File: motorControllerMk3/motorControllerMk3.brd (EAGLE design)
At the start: 54.6 x 49.2 mm, 43 parts, among them J1 AVR_SPI_PRG_6NS, Y1 16MHz

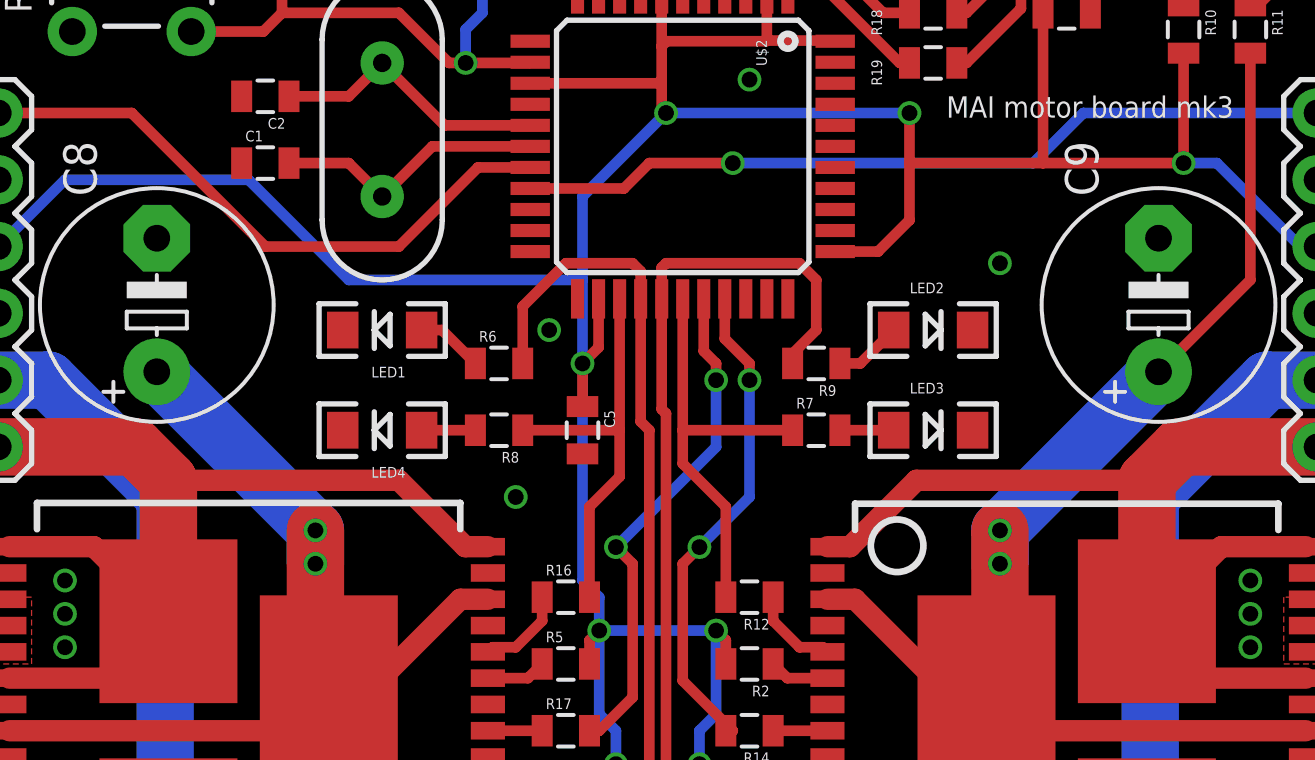
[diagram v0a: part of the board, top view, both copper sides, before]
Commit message: making ground plane bigger
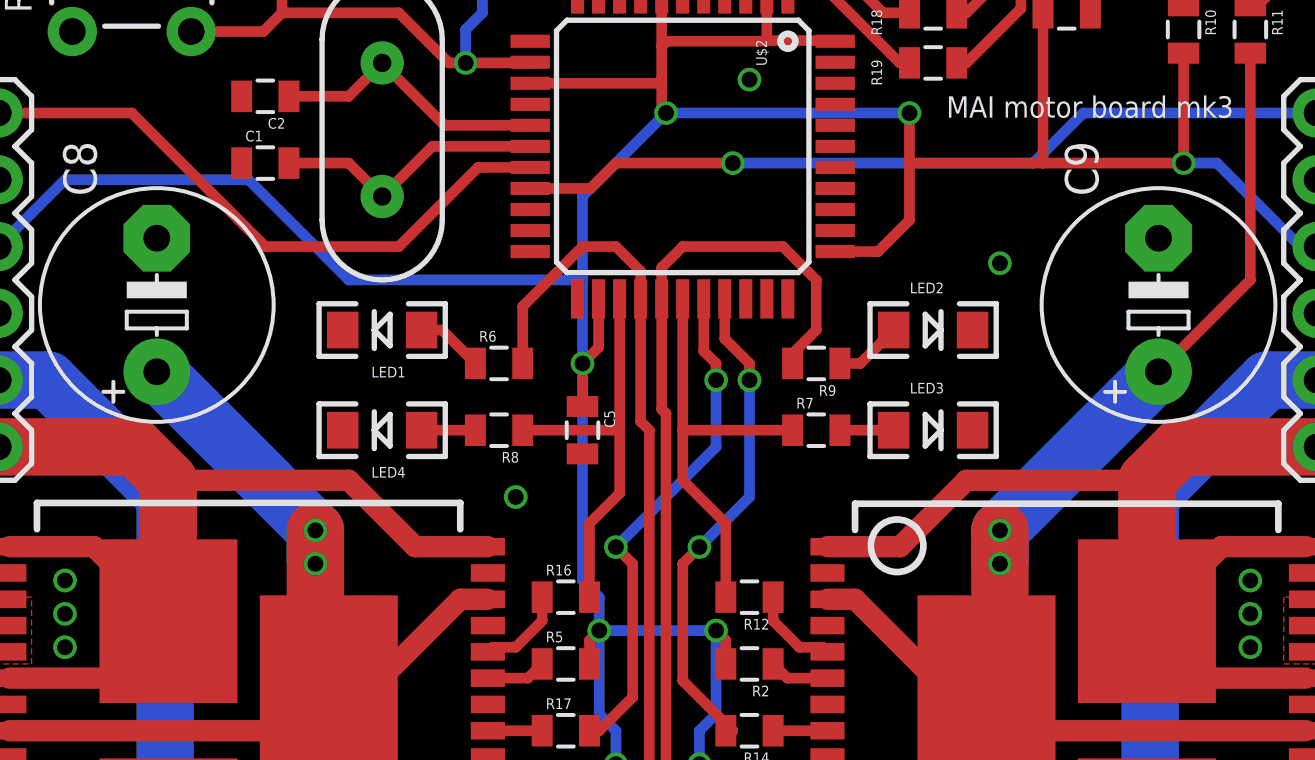
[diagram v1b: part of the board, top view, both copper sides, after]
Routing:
- net PD6: track 31.5 -> 32.0 mm
- net PD7: track 33.8 -> 34.4 mm
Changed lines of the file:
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@@
 <?xml version="1.0" encoding="utf-8"?>
 <!DOCTYPE eagle SYSTEM "eagle.dtd">
-<eagle version="6.3">
+<eagle version="6.5.0">
 <drawing>
 <settings>
@@
 <via x="73.025" y="26.035" extent="1-16" drill="0.6" shape="square"/>
 <via x="73.025" y="27.305" extent="1-16" drill="0.6" shape="square"/>
-<via x="46.355" y="36.83" extent="1-16" drill="0.6" shape="square"/>
 <via x="45.085" y="30.48" extent="1-16" drill="0.6" shape="square"/>
 </signal>
@@
 <wire x1="29.04" y1="28.59" x2="31.875" y2="25.755" width="0.8128" layer="1"/>
 <wire x1="31.89" y1="28.59" x2="31.875" y2="28.575" width="0.8128" layer="1"/>
-<wire x1="44.025" y1="28.59" x2="43.165" y2="28.59" width="0.8128" layer="1"/>
-<wire x1="43.165" y1="28.59" x2="40.64" y2="31.115" width="0.8128" layer="1"/>
-<wire x1="40.64" y1="31.115" x2="31.875" y2="31.115" width="0.8128" layer="1"/>
+<wire x1="44.025" y1="28.59" x2="41.26" y2="28.59" width="0.8128" layer="1"/>
+<wire x1="41.26" y1="28.59" x2="38.735" y2="31.115" width="0.8128" layer="1"/>
+<wire x1="38.735" y1="31.115" x2="31.875" y2="31.115" width="0.8128" layer="1"/>
 <wire x1="25.4" y1="32.385" x2="30.605" y2="32.385" width="2.1844" layer="1"/>
 <wire x1="30.605" y1="32.385" x2="31.875" y2="31.115" width="2.1844" layer="1"/>
@@
 </signal>
 <signal name="PD1">
-<wire x1="49.2" y1="42.215" x2="50.165" y2="43.18" width="0.4064" layer="1"/>
-<wire x1="50.165" y1="43.18" x2="53.34" y2="43.18" width="0.4064" layer="1"/>
+<wire x1="47.93" y1="42.215" x2="48.895" y2="43.18" width="0.4064" layer="1"/>
+<wire x1="48.895" y1="43.18" x2="53.34" y2="43.18" width="0.4064" layer="1"/>
 <via x="53.34" y="43.18" extent="1-16" drill="0.6" shape="square"/>
 <contactref element="JP1" pad="6"/>
 <contactref element="U$2" pad="19"/>
-<wire x1="49.2" y1="42.215" x2="45.635" y2="42.215" width="0.4064" layer="1"/>
+<wire x1="47.93" y1="42.215" x2="45.635" y2="42.215" width="0.4064" layer="1"/>
 <wire x1="53.34" y1="43.18" x2="64.77" y2="43.18" width="0.4064" layer="16"/>
 <wire x1="64.77" y1="43.18" x2="66.675" y2="45.085" width="0.4064" layer="16"/>
@@
 <contactref element="R8" pad="1"/>
 <contactref element="R16" pad="2"/>
-<wire x1="49.035" y1="33.02" x2="49.035" y2="31.255" width="0.4064" layer="1"/>
+<wire x1="49.035" y1="33.02" x2="49.035" y2="30.62" width="0.4064" layer="1"/>
 <wire x1="45.35" y1="33.02" x2="49.035" y2="33.02" width="0.4064" layer="1"/>
 <contactref element="U$2" pad="25"/>
 <wire x1="49.035" y1="38.015" x2="49.035" y2="33.02" width="0.4064" layer="1"/>
-<wire x1="47.89" y1="26.67" x2="47.89" y2="30.11" width="0.4064" layer="1"/>
-<wire x1="47.89" y1="30.11" x2="49.035" y2="31.255" width="0.4064" layer="1"/>
+<wire x1="47.89" y1="26.67" x2="47.89" y2="29.475" width="0.4064" layer="1"/>
+<wire x1="47.89" y1="29.475" x2="49.035" y2="30.62" width="0.4064" layer="1"/>
 </signal>
 <signal name="PB4">
 <contactref element="R7" pad="1"/>
 <contactref element="R12" pad="2"/>
-<wire x1="51.435" y1="33.02" x2="51.435" y2="31.75" width="0.4064" layer="1"/>
+<wire x1="51.435" y1="33.02" x2="51.435" y2="31.115" width="0.4064" layer="1"/>
 <wire x1="55.615" y1="33.02" x2="51.435" y2="33.02" width="0.4064" layer="1"/>
 <contactref element="U$2" pad="28"/>
 <wire x1="51.435" y1="38.015" x2="51.435" y2="33.02" width="0.4064" layer="1"/>
-<wire x1="53.075" y1="26.67" x2="53.075" y2="30.11" width="0.4064" layer="1"/>
-<wire x1="53.075" y1="30.11" x2="51.435" y2="31.75" width="0.4064" layer="1"/>
+<wire x1="53.075" y1="26.67" x2="53.075" y2="29.475" width="0.4064" layer="1"/>
+<wire x1="53.075" y1="29.475" x2="51.435" y2="31.115" width="0.4064" layer="1"/>
 </signal>
 <signal name="PD6">
@@
 <wire x1="50.165" y1="19.05" x2="47.625" y2="16.51" width="0.4064" layer="1"/>
 <wire x1="47.625" y1="16.51" x2="47.89" y2="16.51" width="0.4064" layer="1"/>
-<wire x1="49.835" y1="39.065" x2="49.53" y2="39.37" width="0.4064" layer="1"/>
-<wire x1="49.53" y1="39.37" x2="46.99" y2="39.37" width="0.4064" layer="1"/>
+<wire x1="49.835" y1="39.065" x2="48.895" y2="40.005" width="0.4064" layer="1"/>
+<wire x1="48.895" y1="40.005" x2="47.625" y2="40.005" width="0.4064" layer="1"/>
 <contactref element="U$2" pad="26"/>
 <wire x1="49.835" y1="38.015" x2="49.835" y2="39.065" width="0.4064" layer="1"/>
 <wire x1="49.835" y1="33.35" x2="49.835" y2="38.015" width="0.4064" layer="1"/>
 <wire x1="45.35" y1="35.56" x2="45.35" y2="37.73" width="0.4064" layer="1"/>
-<wire x1="45.35" y1="37.73" x2="46.99" y2="39.37" width="0.4064" layer="1"/>
+<wire x1="45.35" y1="37.73" x2="47.625" y2="40.005" width="0.4064" layer="1"/>
 </signal>
 <signal name="PD7">
@@
 <wire x1="55.615" y1="35.93" x2="56.515" y2="36.83" width="0.4064" layer="1"/>
 <wire x1="56.515" y1="36.83" x2="56.515" y2="38.735" width="0.4064" layer="1"/>
-<wire x1="56.515" y1="38.735" x2="55.88" y2="39.37" width="0.4064" layer="1"/>
-<wire x1="55.88" y1="39.37" x2="50.8" y2="39.37" width="0.4064" layer="1"/>
+<wire x1="56.515" y1="38.735" x2="55.245" y2="40.005" width="0.4064" layer="1"/>
+<wire x1="55.245" y1="40.005" x2="51.435" y2="40.005" width="0.4064" layer="1"/>
 <wire x1="50.635" y1="38.015" x2="50.635" y2="39.205" width="0.4064" layer="1"/>
-<wire x1="50.635" y1="39.205" x2="50.8" y2="39.37" width="0.4064" layer="1"/>
+<wire x1="50.635" y1="39.205" x2="51.435" y2="40.005" width="0.4064" layer="1"/>
 </signal>
 <signal name="N$22">
@@
 <wire x1="71.925" y1="28.59" x2="69.09" y2="25.755" width="0.8128" layer="1"/>
 <wire x1="69.075" y1="28.59" x2="69.09" y2="28.575" width="0.8128" layer="1"/>
-<wire x1="56.94" y1="28.59" x2="57.8" y2="28.59" width="0.8128" layer="1"/>
-<wire x1="57.8" y1="28.59" x2="60.325" y2="31.115" width="0.8128" layer="1"/>
-<wire x1="60.325" y1="31.115" x2="69.09" y2="31.115" width="0.8128" layer="1"/>
+<wire x1="56.94" y1="28.59" x2="59.705" y2="28.59" width="0.8128" layer="1"/>
+<wire x1="59.705" y1="28.59" x2="62.23" y2="31.115" width="0.8128" layer="1"/>
+<wire x1="62.23" y1="31.115" x2="69.09" y2="31.115" width="0.8128" layer="1"/>
 <wire x1="75.565" y1="32.385" x2="70.36" y2="32.385" width="2.1844" layer="1"/>
 <wire x1="70.36" y1="32.385" x2="69.09" y2="31.115" width="2.1844" layer="1"/>

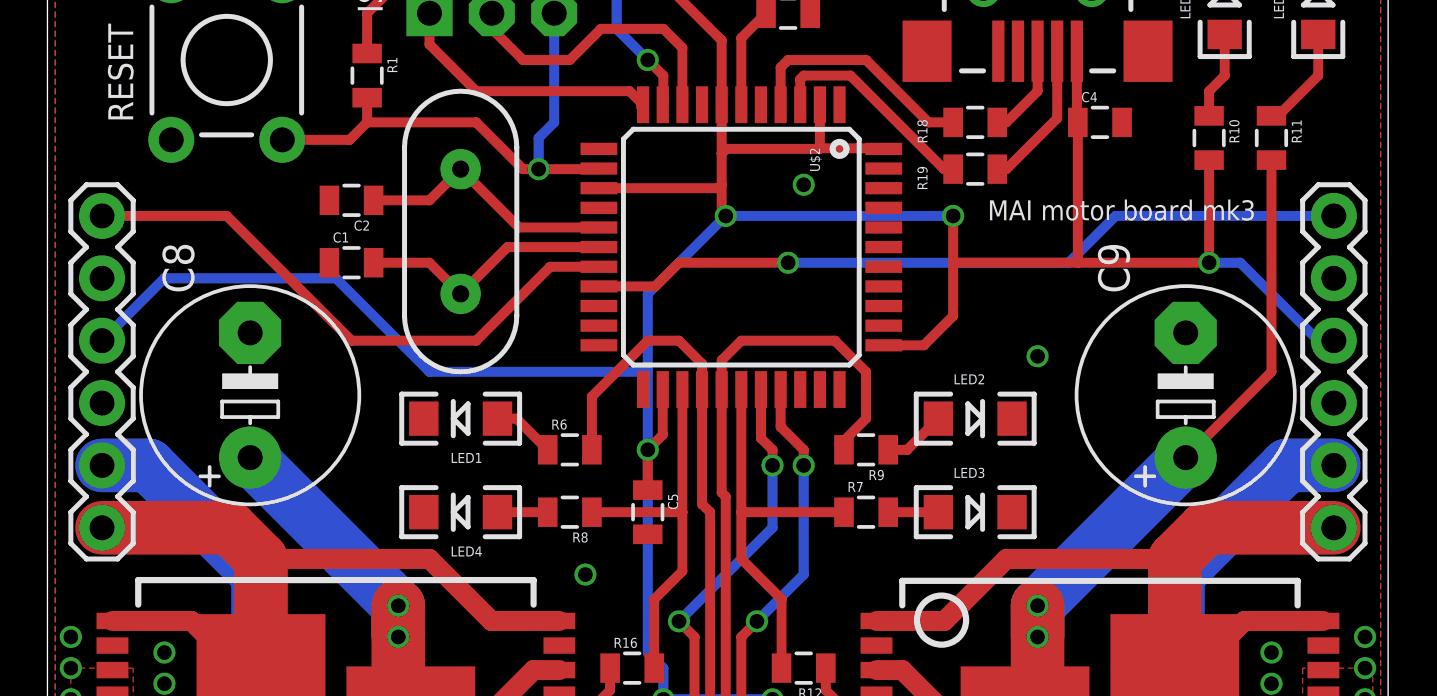
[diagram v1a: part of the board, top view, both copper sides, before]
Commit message: making better silkscreen
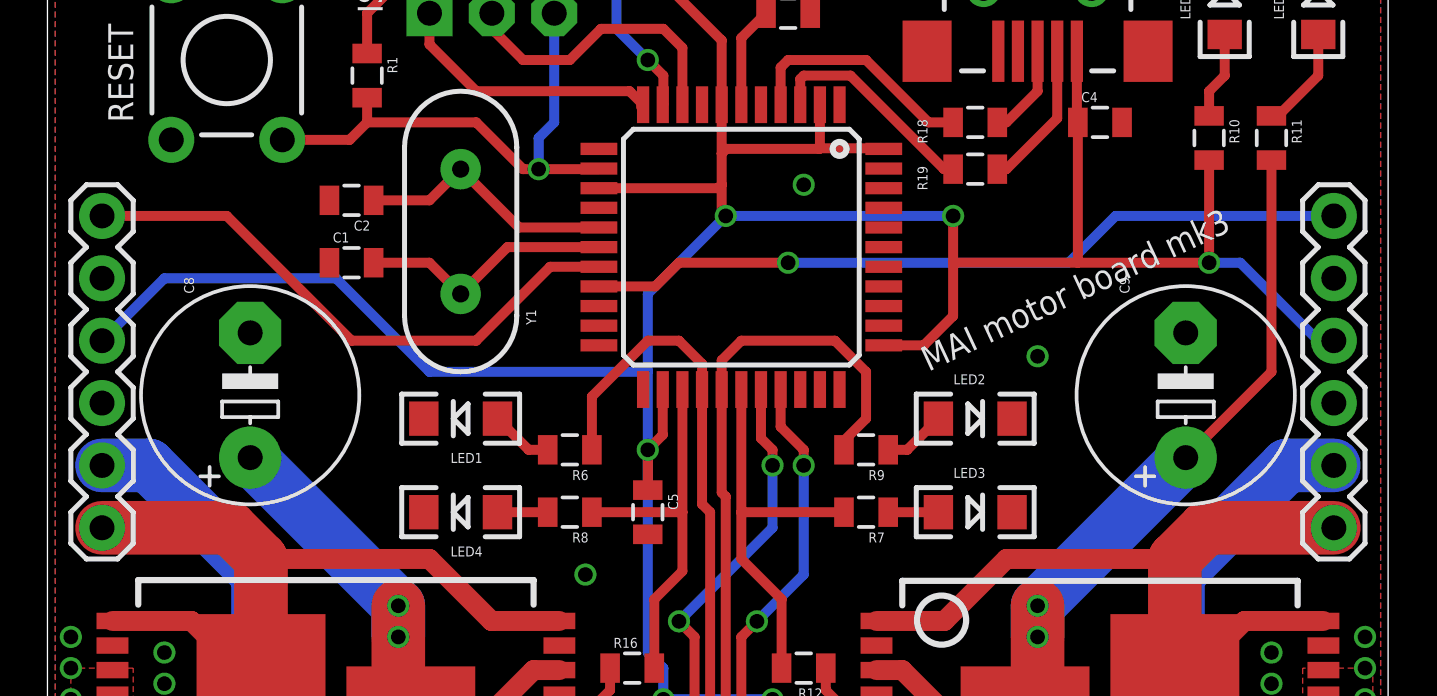
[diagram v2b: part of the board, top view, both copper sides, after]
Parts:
- turned R6 to 180 degrees
- turned R7 to 180 degrees
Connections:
- removed net N$27: LED3.A, R7.2
- removed net N$31: LED1.A, R6.1
- new net N$16: LED3.A, R7.1
- new net N$18: LED1.A, R6.2
- net PB4: now also R7.2; no longer R7.1
- net PD6: now also R6.1; no longer R6.2
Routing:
- net N$31: track 2.57 -> 0.00 mm
- net N$18: track 0.00 -> 2.57 mm
- net N$27: track 2.05 -> 0.00 mm
- net N$16: track 0.00 -> 2.05 mm
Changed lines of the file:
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@@
 <text x="36.83" y="53.34" size="1.016" layer="25" rot="R90">ISP</text>
 <text x="26.67" y="48.895" size="1.016" layer="25" rot="R90">RESET</text>
-<text x="72.39" y="45.72" size="0.8128" layer="21" font="vector" rot="R180">MAI motor board mk3</text>
+<text x="59.055" y="38.735" size="1.016" layer="21" font="vector" rot="R25">MAI motor board mk3</text>
 </plain>
 <attributes>
@@
 <element name="LED3" library="SparkFun-LED" package="LED-1206" value="A1" x="60.96" y="33.02"/>
 <element name="LED4" library="SparkFun-LED" package="LED-1206" value="B2" x="40.005" y="33.02" rot="R180"/>
-<element name="R6" library="SparkFun-Passives" package="0805" value="1k" x="44.45" y="35.56"/>
-<element name="R7" library="SparkFun-Passives" package="0805" value="1k" x="56.515" y="33.02"/>
+<element name="R6" library="SparkFun-Passives" package="0805" value="1k" x="44.45" y="35.56" rot="R180"/>
+<element name="R7" library="SparkFun-Passives" package="0805" value="1k" x="56.515" y="33.02" rot="R180"/>
 <element name="R8" library="SparkFun-Passives" package="0805" value="1k" x="44.45" y="33.02" rot="R180"/>
 <element name="R9" library="SparkFun-Passives" package="0805" value="1k" x="56.515" y="35.56" rot="R180"/>
@@
 <element name="R16" library="SparkFun-Passives" package="0805" value="1k" x="46.99" y="26.67"/>
 <element name="R17" library="SparkFun-Passives" package="0805" value="1k" x="46.99" y="21.59"/>
-<element name="C8" library="rcl" package="E5-8,5" value="2200u" x="31.4325" y="37.7825" rot="R90"/>
-<element name="C9" library="rcl" package="E5-8,5" value="2200u" x="69.5325" y="37.7825" rot="R90"/>
+<element name="C8" library="rcl" package="E5-8,5" value="2200u" x="31.4325" y="37.7825" smashed="yes" rot="R90">
+<attribute name="NAME" x="29.1465" y="41.9227" size="0.4064" layer="25" ratio="10" rot="R90"/>
+<attribute name="VALUE" x="34.4551" y="35.2679" size="0.4064" layer="27" ratio="10" rot="R90"/>
+</element>
+<element name="C9" library="rcl" package="E5-8,5" value="2200u" x="69.5325" y="37.7825" smashed="yes" rot="R90">
+<attribute name="NAME" x="67.2465" y="41.9227" size="0.4064" layer="25" ratio="10" rot="R90"/>
+<attribute name="VALUE" x="72.5551" y="35.2679" size="0.4064" layer="27" ratio="10" rot="R90"/>
+</element>
 <element name="JP1" library="SparkFun-Connectors" package="1X06" value="m1" x="75.565" y="32.385" smashed="yes" rot="R90"/>
 <element name="JP2" library="SparkFun-Connectors" package="1X06" value="m2" x="25.4" y="32.385" smashed="yes" rot="R90"/>
-<element name="U$2" library="SparkFun-DigitalIC" package="SPARKFUN-DIGITALIC_TQFP44" value="ATMEGA32U4TQFP" x="51.435" y="43.815" rot="R270">
+<element name="U$2" library="SparkFun-DigitalIC" package="SPARKFUN-DIGITALIC_TQFP44" value="ATMEGA32U4TQFP" x="51.435" y="43.815" smashed="yes" rot="R270">
 <attribute name="PROD_ID" value="IC-11161" x="51.435" y="43.815" size="1.778" layer="27" rot="R270" display="off"/>
+<attribute name="VALUE" x="47.371" y="47.879" size="0.4064" layer="27" rot="R270"/>
 </element>
 <element name="S2" library="SparkFun-Electromechanical" package="TACTILE-PTH" value="SWITCH-MOMENTARY-2PTH" x="30.48" y="51.435" smashed="yes" rot="R90"/>
-<element name="Y1" library="SparkFun-FreqCtrl" package="HC49US" value="16MHz" x="40.005" y="44.45" smashed="yes" rot="R270"/>
+<element name="Y1" library="SparkFun-FreqCtrl" package="HC49US" value="16MHz" x="40.005" y="44.45" smashed="yes" rot="R270">
+<attribute name="VALUE" x="36.703" y="41.91" size="0.4064" layer="27" ratio="10" rot="R270"/>
+<attribute name="NAME" x="42.672" y="41.275" size="0.4064" layer="25" ratio="10" rot="R270"/>
+</element>
 <element name="U$1" library="SparkFun-PowerIC" package="VNH2SP30" value="VNH2SP30" x="34.925" y="21.59" smashed="yes" rot="R90"/>
 <element name="U$3" library="SparkFun-PowerIC" package="VNH2SP30" value="VNH2SP30" x="66.04" y="21.59" smashed="yes" rot="R270"/>
@@
 </signal>
 <signal name="PB4">
-<contactref element="R7" pad="1"/>
 <contactref element="R12" pad="2"/>
-<wire x1="51.435" y1="33.02" x2="51.435" y2="31.115" width="0.4064" layer="1"/>
-<wire x1="55.615" y1="33.02" x2="51.435" y2="33.02" width="0.4064" layer="1"/>
 <contactref element="U$2" pad="28"/>
 <wire x1="51.435" y1="38.015" x2="51.435" y2="33.02" width="0.4064" layer="1"/>
+<wire x1="51.435" y1="33.02" x2="51.435" y2="31.115" width="0.4064" layer="1"/>
 <wire x1="53.075" y1="26.67" x2="53.075" y2="29.475" width="0.4064" layer="1"/>
 <wire x1="53.075" y1="29.475" x2="51.435" y2="31.115" width="0.4064" layer="1"/>
+<contactref element="R7" pad="2"/>
+<wire x1="55.615" y1="33.02" x2="51.435" y2="33.02" width="0.4064" layer="1"/>
 </signal>
 <signal name="PD6">
-<contactref element="R6" pad="2"/>
 <contactref element="R15" pad="2"/>
 <wire x1="49.835" y1="33.35" x2="50.165" y2="33.02" width="0.4064" layer="1"/>
@@
 <wire x1="49.835" y1="38.015" x2="49.835" y2="39.065" width="0.4064" layer="1"/>
 <wire x1="49.835" y1="33.35" x2="49.835" y2="38.015" width="0.4064" layer="1"/>
+<wire x1="45.35" y1="37.73" x2="47.625" y2="40.005" width="0.4064" layer="1"/>
+<contactref element="R6" pad="1"/>
 <wire x1="45.35" y1="35.56" x2="45.35" y2="37.73" width="0.4064" layer="1"/>
-<wire x1="45.35" y1="37.73" x2="47.625" y2="40.005" width="0.4064" layer="1"/>
 </signal>
 <signal name="PD7">
@@
 <wire x1="41.505" y1="33.02" x2="43.55" y2="33.02" width="0.4064" layer="1"/>
 </signal>
-<signal name="N$27">
-<contactref element="LED3" pad="A"/>
-<contactref element="R7" pad="2"/>
-<wire x1="59.46" y1="33.02" x2="57.415" y2="33.02" width="0.4064" layer="1"/>
-</signal>
 <signal name="N$30">
 <contactref element="LED2" pad="A"/>
@@
 <wire x1="57.415" y1="35.56" x2="58.19" y2="35.56" width="0.4064" layer="1"/>
 <wire x1="58.19" y1="35.56" x2="59.46" y2="36.83" width="0.4064" layer="1"/>
-</signal>
-<signal name="N$31">
-<contactref element="LED1" pad="A"/>
-<contactref element="R6" pad="1"/>
-<wire x1="41.505" y1="36.83" x2="42.28" y2="36.83" width="0.4064" layer="1"/>
-<wire x1="42.28" y1="36.83" x2="43.55" y2="35.56" width="0.4064" layer="1"/>
 </signal>
 <signal name="N$28">
@@
 <wire x1="62.23" y1="46.99" x2="61.86" y2="46.99" width="0.4064" layer="1"/>
 </signal>
+<signal name="N$16">
+<contactref element="R7" pad="1"/>
+<contactref element="LED3" pad="A"/>
+<wire x1="57.415" y1="33.02" x2="59.46" y2="33.02" width="0.4064" layer="1"/>
+</signal>
+<signal name="N$18">
+<contactref element="LED1" pad="A"/>
+<contactref element="R6" pad="2"/>
+<wire x1="43.55" y1="35.56" x2="42.775" y2="35.56" width="0.4064" layer="1"/>
+<wire x1="42.775" y1="35.56" x2="41.505" y2="36.83" width="0.4064" layer="1"/>
+</signal>
 </signals>
